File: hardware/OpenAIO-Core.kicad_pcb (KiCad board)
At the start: 6 copper layers, 23 x 20.1 mm, 87 parts, among them J23 5V, J26 5V, J30 5V, J34 5V, J35 5V, J37 5V, J38 5V, J39 5V, J40 5V, J41 5V, J42 5V, J43 5V, J44 5V, J45 5V, J48 5V, J49 5V, J50 5V, J51 5V, J52 5V, J53 5V, J54 5V, J55 5V, J91 Core_LGA, Q1 AP1606, Q2 AP1606, U1 TS2306A 240GF MSM 9_C2976675, U10 COS8051SOT, U11 TLV7031DPWR, U2 RP2354A, U6 LP5912-1.8DRVR, U8 BMI270, U9 SN74LVC1G3157DTBR, X1 XTM25012000JT00351001

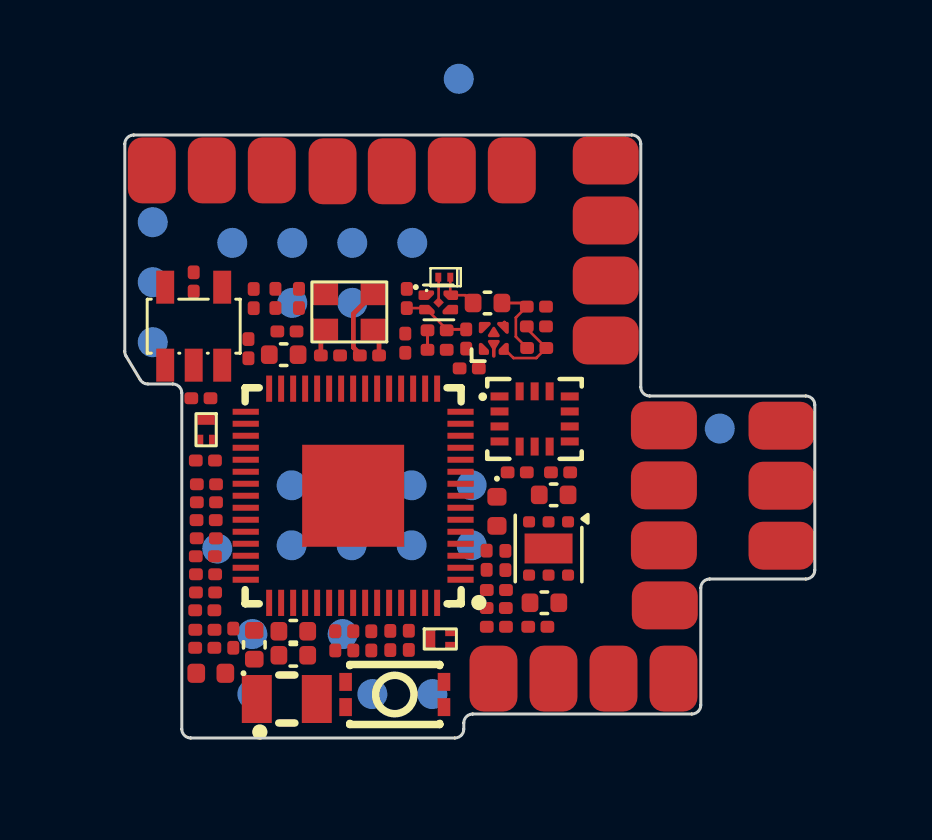
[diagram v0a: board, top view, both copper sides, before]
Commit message: OpenAIO: new marker test points TP29 (BUZZER-) and TP30 (+5V) on the Base; lga_apply only excludes the markers it consumed
Co-Authored-By: Claude Fable 5 <noreply@anthropic.com>
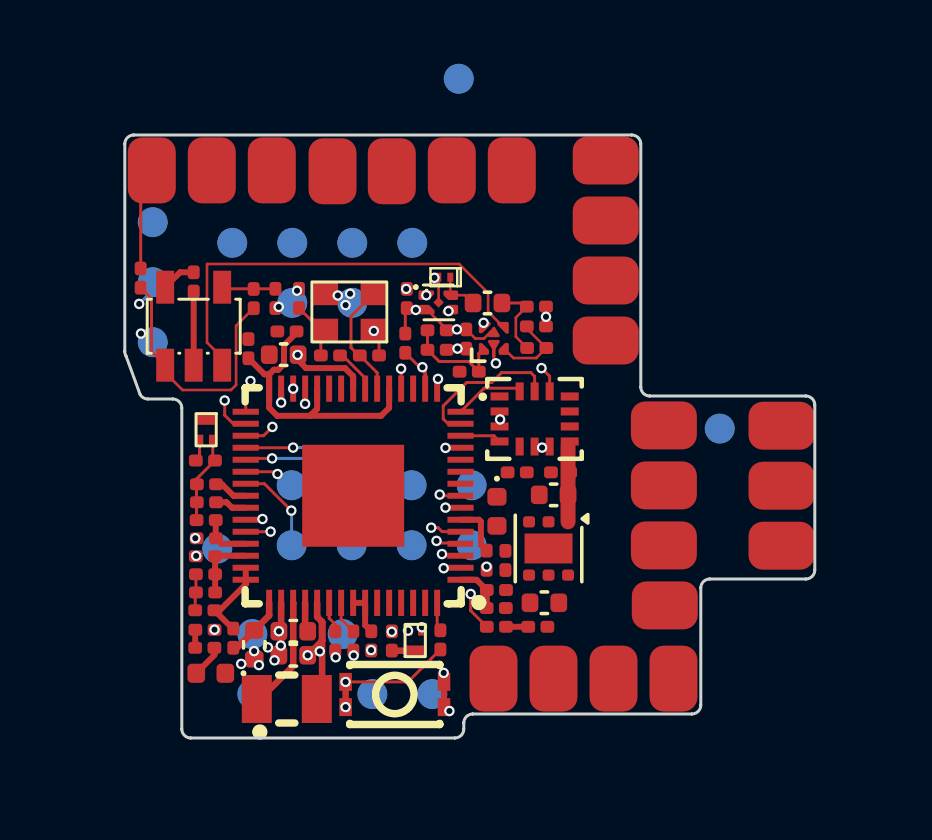
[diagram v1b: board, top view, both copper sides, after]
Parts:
- moved R33 4.48 mm to (103.6, 48.3), turned to 90 degrees
- moved R7 1.67 mm to (113.6, 60.3)
- moved Q2 0.84 mm to (112.8, 60.4), turned to 90 degrees
- moved R14 0.57 mm to (112.0, 60.4), turned to -90 degrees
- moved R27 0.11 mm to (114.6, 51.4)
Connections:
- U2 pad 24: unconnected-(U2-SWCLK-Pad24) -> (no net)
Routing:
- net +3.3V: track 2.43 -> 24.5 mm, vias 0 -> 2
- net Net-(U10-IN+): track 0.18 -> 14.7 mm
- net GND: track 2.57 -> 13.5 mm, vias 0 -> 26
- net +1.1V: track 0.00 -> 9.81 mm, vias 0 -> 3
- net Net-(U10-OUT): track 0.00 -> 8.64 mm
- net MOTOR3: track 0.00 -> 5.52 mm, vias 0 -> 1
- net /IMU/SPI1.SCK: track 0.00 -> 5.13 mm
- net Net-(R7-Pad1): track 0.00 -> 4.45 mm, vias 0 -> 2
- net MOTOR4: track 0.00 -> 4.05 mm, vias 0 -> 1
- net Net-(U2-VREG_LX): track 0.00 -> 3.78 mm
- net /OSD/VIDEO_OUT: track 0.00 -> 3.42 mm
- net /IMU/CS: track 0.00 -> 3.11 mm, vias 0 -> 2
- net MOTOR1: track 0.00 -> 3.05 mm, vias 0 -> 1
- net /OSD/OSD_LVL: track 0.65 -> 3.37 mm
- net +1.8V_GYRO: track 0.00 -> 2.52 mm
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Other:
- outline, holes or cut-outs redrawn

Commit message: OpenAIO: LGA 31 pins (+5V and BUZZER- added, stray GND removed), J91 follows the pattern centre automatically
Co-Authored-By: Claude Fable 5 <noreply@anthropic.com>
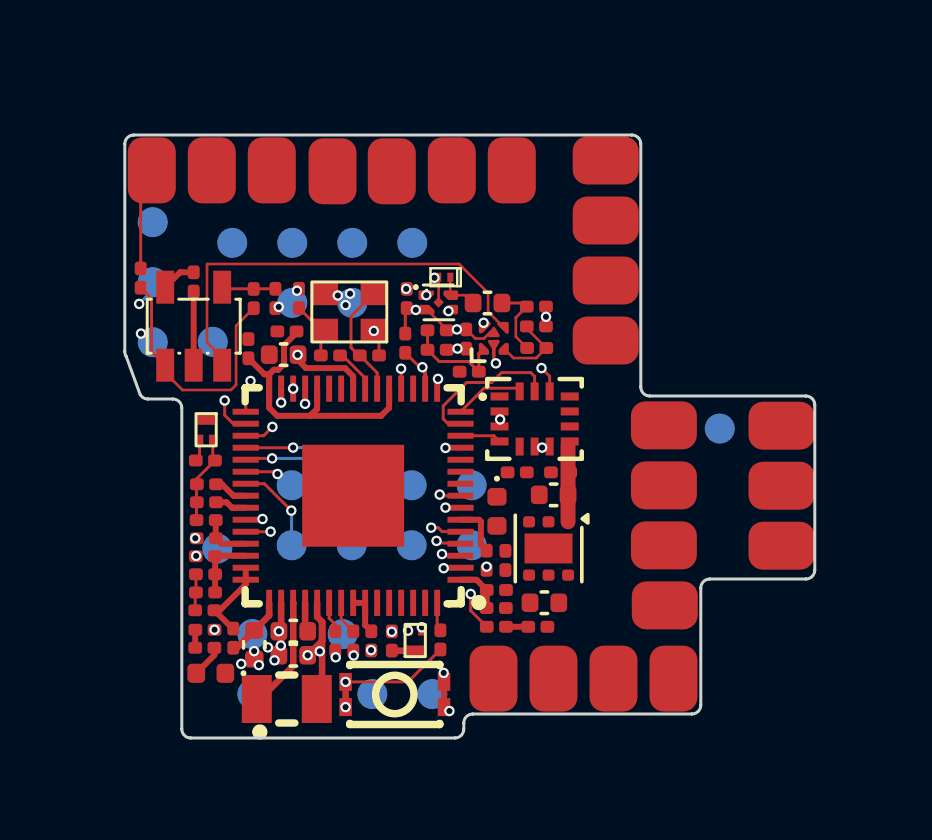
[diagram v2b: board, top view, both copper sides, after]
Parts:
- moved J91 1.39 mm to (114.5, 53.3)
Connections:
- J91 pad 1: GND -> 10V_ENABLE
- J91 pad 10: GND -> USB_D-
- J91 pad 11: USB_D- -> +5V
- J91 pad 18: MOTOR1 -> BUZZER-
- J91 pad 19: MOTOR3 -> MOTOR1
- J91 pad 2: 10V_ENABLE -> CURR
- J91 pad 20: GND -> MOTOR3
- J91 pad 22: +BATT -> GND
- J91 pad 23: GND -> +BATT
- J91 pad 26: UART0_TX -> GND
- J91 pad 27: UART0_RX -> UART0_TX
- J91 pad 28: LED_STRIP -> UART0_RX
- J91 pad 29: UART1_RX -> LED_STRIP
- J91 pad 3: CURR -> SPI0.MISO
- J91 pad 30: UART1_TX -> UART1_RX
- J91 pad 4: SPI0.MISO -> SPI0.SCK
- J91 pad 5: SPI0.SCK -> SPI0.MOSI
- J91 pad 6: SPI0.MOSI -> FLASH_CS
- J91 pad 7: FLASH_CS -> USB_D+
- J91 pad 8: USB_D+ -> GND
- Q1 pad 3: /Pads/BUZZER- -> BUZZER-
- U2 pad 24: (no net) -> unconnected-(U2-SWCLK-Pad24)
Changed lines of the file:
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@@
 		(capping no)
 		(filling no)
-		(aux_axis_origin 114.481924 51.885797)
+		(aux_axis_origin 114.481924 53.275797)
 		(pcbplotparams
 			(layerselection 0x00000000_00000000_55555555_5755f5ff)
@@
 			(size 0.6 0.35)
 			(layers "F.Cu" "F.Mask" "F.Paste")
-			(net "/Pads/BUZZER-")
+			(net "BUZZER-")
 			(pinfunction "D_3")
 			(pintype "unspecified")
@@
 			(size 0.2 0.875)
 			(layers "F.Cu" "F.Mask" "F.Paste")
+			(net "unconnected-(U2-SWCLK-Pad24)")
 		)
 		(pad "25" smd rect
@@
 	(footprint "lib:Core_LGA_pads"
 		(layer "B.Cu")
-		(at 114.481924 51.885797 180)
+		(at 114.481924 53.275797 180)
 		(descr "OpenAIO Core LGA pads on the Core bottom. Place on B.Cu: X is pre-mirrored so the flipped footprint overlays Core_LGA_land pad for pad. No paste. Generated by tools/lga_gen.py")
 		(tags "OpenAIO LGA board-to-board")
 		(property "Reference" "J91"
-			(at 0 12.01 0)
+			(at 0 10.62 0)
 			(unlocked yes)
 			(layer "B.SilkS")
@@
 		)
 		(property "Value" "Core_LGA"
-			(at 0 -12.01 0)
+			(at 0 -10.62 0)
 			(unlocked yes)
 			(layer "B.Fab")
@@
 		(duplicate_pad_numbers_are_jumpers no)
 		(fp_circle
-			(center 1.15 11.16)
-			(end 1.3 11.16)
+			(center 11.35 9.77)
+			(end 11.5 9.77)
 			(stroke
 				(width 0.15)
@@
 		)
 		(fp_rect
-			(start -11.2 11.01)
-			(end 11.2 -11.01)
+			(start -11.2 9.62)
+			(end 11.2 -9.62)
 			(stroke
 				(width 0.05)
@@
 		)
 		(fp_rect
-			(start -11.2 11.01)
-			(end 11.2 -11.01)
+			(start -11.2 9.62)
+			(end 11.2 -9.62)
 			(stroke
 				(width 0.1)
@@
 		)
 		(fp_circle
-			(center 1.15 11.16)
-			(end 1.3 11.16)
+			(center 11.35 9.77)
+			(end 11.5 9.77)
 			(stroke
 				(width 0.1)
@@
 		)
 		(pad "1" smd circle
-			(at 0.25 10.26 180)
+			(at 10.45 8.87 180)
 			(size 1 1)
 			(layers "B.Cu" "B.Mask")
-			(net "GND")
+			(net "10V_ENABLE")
 		)
 		(pad "2" smd circle
-			(at 10.45 7.48 180)
+			(at 10.45 6.87 180)
 			(size 1 1)
 			(layers "B.Cu" "B.Mask")
-			(net "10V_ENABLE")
+			(net "CURR")
 		)
 		(pad "3" smd circle
-			(at 10.45 5.48 180)
+			(at 7.8 6.18 180)
 			(size 1 1)
 			(layers "B.Cu" "B.Mask")
-			(net "CURR")
+			(net "SPI0.MISO")
 		)
 		(pad "4" smd circle
-			(at 7.8 4.79 180)
+			(at 5.8 6.18 180)
 			(size 1 1)
 			(layers "B.Cu" "B.Mask")
-			(net "SPI0.MISO")
+			(net "SPI0.SCK")
 		)
 		(pad "5" smd circle
-			(at 5.8 4.79 180)
+			(at 3.8 6.18 180)
 			(size 1 1)
 			(layers "B.Cu" "B.Mask")
-			(net "SPI0.SCK")
+			(net "SPI0.MOSI")
 		)
 		(pad "6" smd circle
-			(at 3.8 4.79 180)
+			(at 1.8 6.18 180)
 			(size 1 1)
 			(layers "B.Cu" "B.Mask")
-			(net "SPI0.MOSI")
+			(net "FLASH_CS")
 		)
 		(pad "7" smd circle
-			(at 1.8 4.79 180)
+			(at 10.45 4.87 180)
 			(size 1 1)
 			(layers "B.Cu" "B.Mask")
-			(net "FLASH_CS")
+			(net "USB_D+")
 		)
 		(pad "8" smd circle
-			(at 10.45 3.48 180)
+			(at 5.8 4.18 180)
 			(size 1 1)
 			(layers "B.Cu" "B.Mask")
-			(net "USB_D+")
+			(net "GND")
 		)
 		(pad "9" smd circle
-			(at 5.8 2.79 180)
+			(at 3.8 4.18 180)
 			(size 1 1)
 			(layers "B.Cu" "B.Mask")
@@
 		)
 		(pad "10" smd circle
-			(at 3.8 2.79 180)
+			(at 10.45 2.87 180)
 			(size 1 1)
 			(layers "B.Cu" "B.Mask")
-			(net "GND")
+			(net "USB_D-")
 		)
 		(pad "11" smd circle
-			(at 10.45 1.48 180)
+			(at 8.45 2.88 180)
 			(size 1 1)
 			(layers "B.Cu" "B.Mask")
-			(net "USB_D-")
+			(net "+5V")
 		)
 		(pad "12" smd circle
-			(at -8.45 -1.4 180)
+			(at -8.45 -0.01 180)
 			(size 1 1)
 			(layers "B.Cu" "B.Mask")
@@
 		)
 		(pad "13" smd circle
-			(at -10.45 -1.4 180)
+			(at -10.45 -0.01 180)
 			(size 1 1)
 			(layers "B.Cu" "B.Mask")
@@
 		)
 		(pad "14" smd circle
-			(at 5.82 -3.29 180)
+			(at 5.82 -1.9 180)
 			(size 1 1)
 			(layers "B.Cu" "B.Mask")
@@
 		)
 		(pad "15" smd circle
-			(at 3.82 -3.29 180)
+			(at 3.82 -1.9 180)
 			(size 1 1)
 			(layers "B.Cu" "B.Mask")
@@
 		)
 		(pad "16" smd circle
-			(at 1.82 -3.29 180)
+			(at 1.82 -1.9 180)
 			(size 1 1)
 			(layers "B.Cu" "B.Mask")
@@
 		)
 		(pad "17" smd circle
-			(at -0.18 -3.29 180)
+			(at -0.18 -1.9 180)
 			(size 1 1)
 			(layers "B.Cu" "B.Mask")
@@
 		)
 		(pad "18" smd circle
-			(at 5.82 -5.29 180)
+			(at -10.45 -2.01 180)
 			(size 1 1)
 			(layers "B.Cu" "B.Mask")
-			(net "MOTOR1")
+			(net "BUZZER-")
 		)
 		(pad "19" smd circle
-			(at 3.82 -5.29 180)
+			(at 5.82 -3.9 180)
 			(size 1 1)
 			(layers "B.Cu" "B.Mask")
-			(net "MOTOR3")
+			(net "MOTOR1")
 		)
 		(pad "20" smd circle
-			(at 1.82 -5.29 180)
+			(at 3.82 -3.9 180)
 			(size 1 1)
 			(layers "B.Cu" "B.Mask")
-			(net "GND")
+			(net "MOTOR3")
 		)
 		(pad "21" smd circle
-			(at -0.18 -5.29 180)
+			(at 1.82 -3.9 180)
 			(size 1 1)
 			(layers "B.Cu" "B.Mask")
@@
 		)
 		(pad "22" smd circle
-			(at 8.3 -5.4 180)
+			(at -0.18 -3.9 180)
 			(size 1 1)
 			(layers "B.Cu" "B.Mask")
-			(net "+BATT")
+			(net "GND")
 		)
 		(pad "23" smd circle
-			(at 7.13 -8.25 180)
+			(at 8.3 -4.01 180)
 			(size 1 1)
 			(layers "B.Cu" "B.Mask")
-			(net "GND")
+			(net "+BATT")
 		)
 		(pad "24" smd circle
-			(at 4.12 -8.25 180)
+			(at 7.13 -6.86 180)
 			(size 1 1)
 			(layers "B.Cu" "B.Mask")
@@
 		)
 		(pad "25" smd circle
-			(at -2.97 -9.95 180)
+			(at 4.12 -6.86 180)
 			(size 1 1)
 			(layers "B.Cu" "B.Mask")
@@
 		)
 		(pad "26" smd circle
-			(at -4.97 -9.95 180)
+			(at -2.97 -8.56 180)
 			(size 1 1)
 			(layers "B.Cu" "B.Mask")
-			(net "UART0_TX")
+			(net "GND")
 		)
 		(pad "27" smd circle
-			(at -6.97 -9.95 180)
+			(at -4.97 -8.56 180)
 			(size 1 1)
 			(layers "B.Cu" "B.Mask")
-			(net "UART0_RX")
+			(net "UART0_TX")
 		)
 		(pad "28" smd circle
-			(at 7.13 -10.25 180)
+			(at -6.97 -8.56 180)
 			(size 1 1)
 			(layers "B.Cu" "B.Mask")
-			(net "LED_STRIP")
+			(net "UART0_RX")
 		)
 		(pad "29" smd circle
-			(at 3.13 -10.25 180)
+			(at 7.13 -8.86 180)
 			(size 1 1)
 			(layers "B.Cu" "B.Mask")
-			(net "UART1_RX")
+			(net "LED_STRIP")
 		)
 		(pad "30" smd circle
-			(at 1.13 -10.25 180)
+			(at 3.13 -8.86 180)
+			(size 1 1)
+			(layers "B.Cu" "B.Mask")
+			(net "UART1_RX")
+		)
+		(pad "31" smd circle
+			(at 1.13 -8.86 180)
 			(size 1 1)
 			(layers "B.Cu" "B.Mask")

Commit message: OpenAIO: LGA +10V pin added
Co-Authored-By: Claude Fable 5 <noreply@anthropic.com>
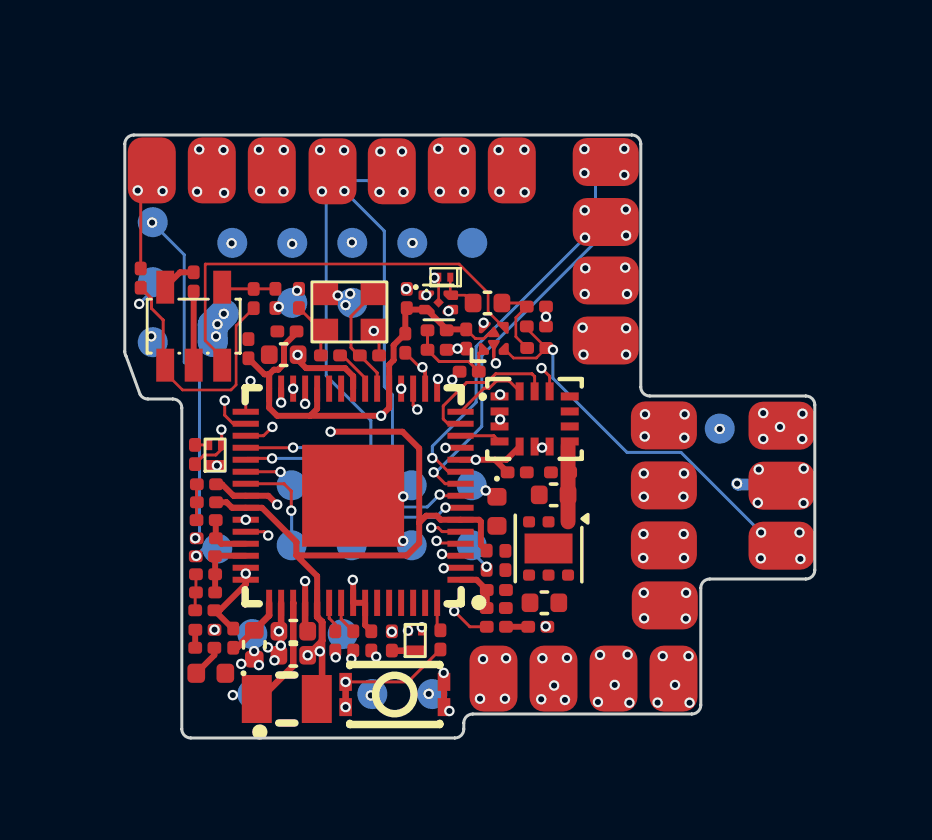
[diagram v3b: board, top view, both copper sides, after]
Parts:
- moved J55 2.05 mm to (119.1, 46.4), turned to 0 degrees
- moved J54 1.95 mm to (119.1, 44.4), turned to 0 degrees
- moved Q1 0.90 mm to (106.1, 54.2), turned to 90 degrees
- moved R13 0.40 mm to (105.4, 54.1), turned to -90 degrees
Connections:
- J91 pad 10: USB_D- -> GND
- J91 pad 11: +5V -> USB_D-
- J91 pad 12: GND -> +5V
- J91 pad 14: MOTOR2 -> GND
- J91 pad 15: MOTOR4 -> MOTOR2
- J91 pad 16: GND -> MOTOR4
- J91 pad 18: BUZZER- -> GND
- J91 pad 19: MOTOR1 -> BUZZER-
- J91 pad 20: MOTOR3 -> MOTOR1
- J91 pad 21: GND -> MOTOR3
- J91 pad 23: +BATT -> GND
- J91 pad 24: GND -> +BATT
- J91 pad 27: UART0_TX -> GND
- J91 pad 28: UART0_RX -> UART0_TX
- J91 pad 29: LED_STRIP -> UART0_RX
- J91 pad 30: UART1_RX -> LED_STRIP
- J91 pad 31: UART1_TX -> UART1_RX
- J91 pad 7: USB_D+ -> +10V
- J91 pad 8: GND -> USB_D+
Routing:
- net /Pads/I2C0.SDA: track 0.50 -> 23.6 mm, vias 1 -> 6
- net UART1_TX: track 0.00 -> 23.1 mm, vias 0 -> 6
- net BUZZER-: track 0.00 -> 20.9 mm, vias 0 -> 2
- net UART1_RX: track 0.00 -> 20.9 mm, vias 0 -> 6
- net /Pads/I2C0.SCL: track 2.02 -> 20.6 mm, vias 2 -> 6
- net +1.1V: track 9.81 -> 26.4 mm, vias 3 -> 4
- net USB_D+: track 1.08 -> 17.3 mm
- net USB_D-: track 0.74 -> 13.7 mm
- net CURR: track 0.05 -> 11.3 mm, vias 1 -> 2
- net /OSD/VIDEO_IN: track 2.65 -> 12.7 mm, vias 0 -> 5
- net SPI0.SCK: track 0.46 -> 9.79 mm, vias 1 -> 2
- net UART0_RX: track 0.64 -> 9.41 mm, vias 1 -> 6
- net FLASH_CS: track 1.01 -> 9.68 mm, vias 1 -> 2
- net /Pads/PU0RX: track 1.03 -> 9.25 mm, vias 1 -> 5
- net /Pads/PIOUART0_TX: track 0.84 -> 8.91 mm, vias 1 -> 5
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
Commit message: OpenAIO: LGA +3.3V pin added
Co-Authored-By: Claude Fable 5 <noreply@anthropic.com>
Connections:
- J91 pad 11: USB_D- -> GND
- J91 pad 12: +5V -> USB_D-
- J91 pad 13: GND -> +5V
- J91 pad 15: MOTOR2 -> GND
- J91 pad 16: MOTOR4 -> MOTOR2
- J91 pad 17: GND -> MOTOR4
- J91 pad 19: BUZZER- -> GND
- J91 pad 20: MOTOR1 -> BUZZER-
- J91 pad 21: MOTOR3 -> MOTOR1
- J91 pad 22: GND -> MOTOR3
- J91 pad 24: +BATT -> GND
- J91 pad 25: GND -> +BATT
- J91 pad 28: UART0_TX -> GND
- J91 pad 29: UART0_RX -> UART0_TX
- J91 pad 30: LED_STRIP -> UART0_RX
- J91 pad 31: UART1_RX -> LED_STRIP
- J91 pad 32: UART1_TX -> UART1_RX
- J91 pad 8: USB_D+ -> +3.3V
- J91 pad 9: GND -> USB_D+
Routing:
- net +5V: track 1.10 -> 47.0 mm
- net +10V: track 0.00 -> 18.4 mm, vias 8 -> 12
- net +4v5: track 0.00 -> 14.4 mm, vias 8 -> 7
- net +3.3V: track 31.5 -> 43.4 mm, vias 6 -> 8
- net +1.1V: track 26.4 -> 29.4 mm
- net LED_STRIP: track 1.45 -> 2.63 mm
- net SPI0.MOSI: track 7.13 -> 7.68 mm
- net /RP2354A/BEEPER: track 5.88 -> 5.36 mm
- net Net-(R7-Pad1): track 4.45 -> 4.22 mm, vias 2 -> 1
- net GND: track 14.8 -> 14.9 mm, vias 56 -> 64
- added copper zone on In3.Cu, net +10V
- added copper zone on In3.Cu, net +3.3V
- added copper zone on In3.Cu, net GND

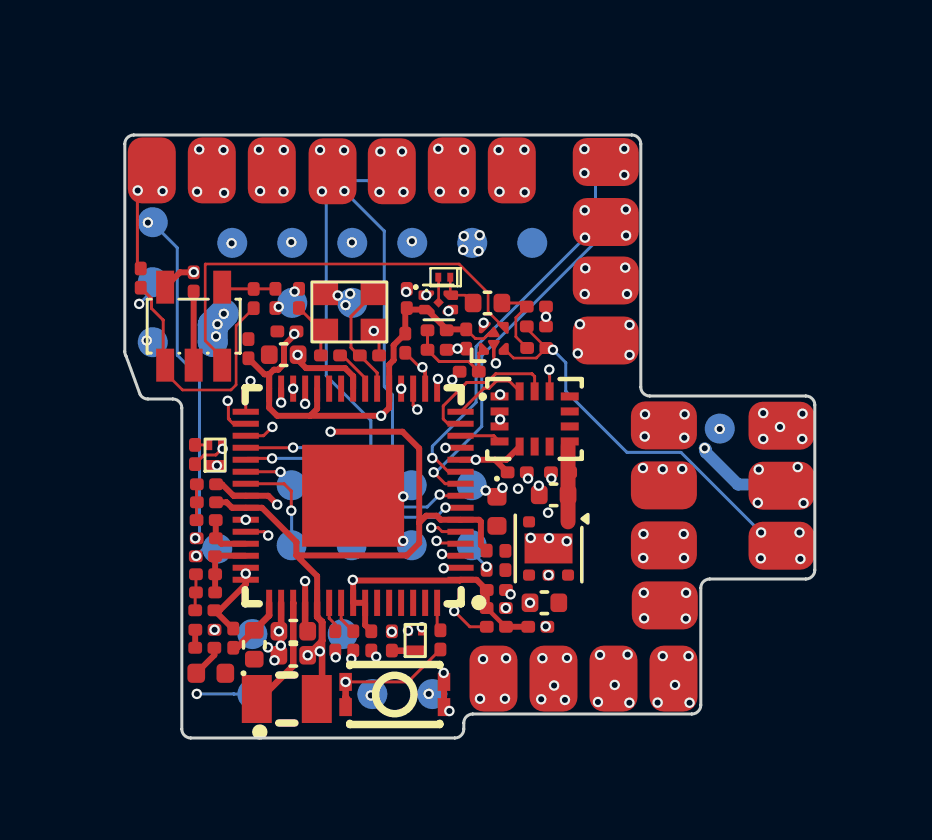
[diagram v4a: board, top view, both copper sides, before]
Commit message: OpenAIO-Core: fully routed by Stan, DRC clean, 0 unconnected
Co-Authored-By: Claude Fable 5 <noreply@anthropic.com>
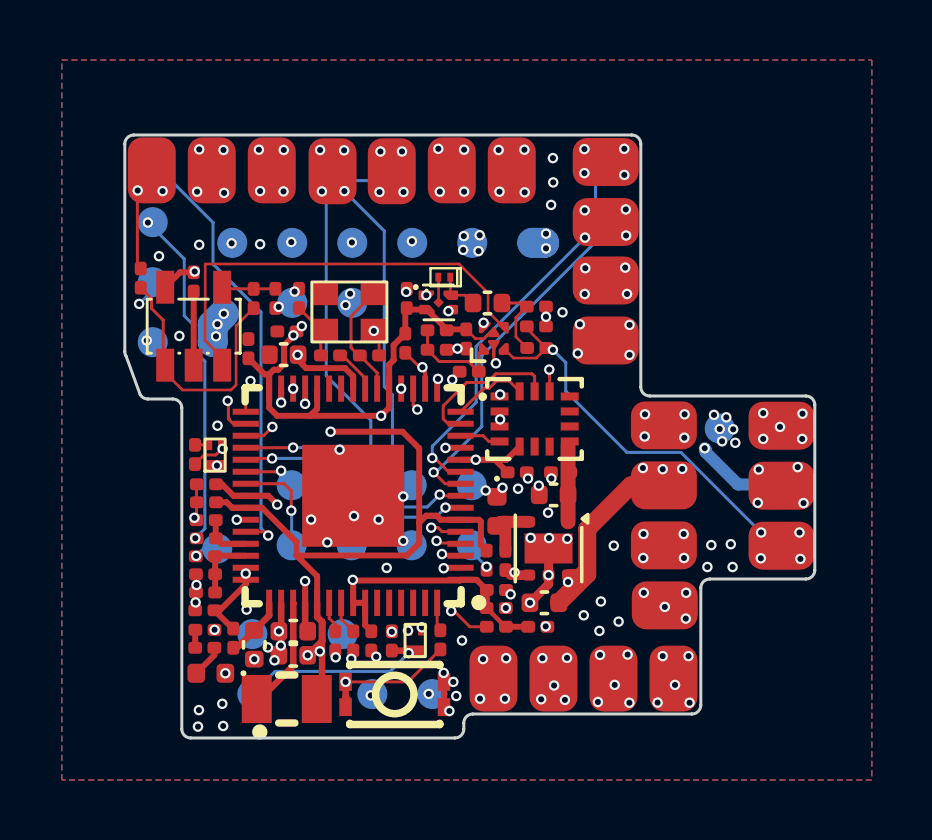
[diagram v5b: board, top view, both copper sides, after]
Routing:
- net +3.3V: track 43.4 -> 58.9 mm, vias 8 -> 11
- net 10V_ENABLE: track 0.80 -> 14.8 mm
- net +4v5: track 14.4 -> 27.3 mm, vias 7 -> 9
- net +5V: track 47.0 -> 56.5 mm
- net /RP2354A/LED0: track 0.00 -> 3.98 mm
- net LED_STRIP: track 2.63 -> 6.55 mm
- net GND: track 14.9 -> 17.5 mm, vias 64 -> 105
- net /Power/1.8V_PG: track 0.00 -> 2.30 mm
- net UART0_RX: track 9.41 -> 10.0 mm
- added copper zone on B.Cu, net GND
- added copper zone on F.Cu, net GND
- added copper zone on In1.Cu, net GND
- added copper zone on In2.Cu, net GND
- added copper zone on In4.Cu, net GND
